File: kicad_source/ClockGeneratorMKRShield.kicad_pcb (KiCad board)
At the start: 2 copper layers, 60 x 23 mm, 3 parts, among them CN1 ARDUINO_MKR

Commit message: generated layout
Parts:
- added C1: 6.8 pF, capacitors:C_0603, F.Cu at (120.0, 167.5)
- added C10: C_0603, capacitors:C_0603, F.Cu at (89.0, 164.5)
- added C11: C_0603, capacitors:C_0603, F.Cu at (94.0, 155.0)
- added C13: C_0603, capacitors:C_0603, F.Cu at (81.0, 167.5)
- added C14: C_0603, capacitors:C_0603, F.Cu at (86.0, 158.5)
- added C16: C_0603, capacitors:C_0603, F.Cu at (72.0, 165.0)
- added C17: C_0603, capacitors:C_0603, F.Cu at (75.3, 155.4)
- added C2: 6.8 pF, capacitors:C_0603, F.Cu at (120.0, 161.5)
- added C3: 100 nF, capacitors:C_0603, F.Cu at (112.0, 161.0)
- added C4: C_0603, capacitors:C_0603, F.Cu at (100.5, 167.5)
- added C5: C_0603, capacitors:C_0603, F.Cu at (105.5, 158.5)
- added C6: C_0603, capacitors:C_0603, F.Cu at (109.4, 158.1)
- added C7: C_0603, capacitors:C_0603, F.Cu at (98.0, 166.5)
- added C8: C_0603, capacitors:C_0603, F.Cu at (103.0, 157.0)
- added CN2: 60312202114509, CON_wuerth:WR-SMA-PCB, F.Cu at (64.0, 162.5)
- added CN3: 60312202114509, CON_wuerth:WR-SMA-PCB, F.Cu at (75.5, 147.5)
- added L10: INDUCTOR_SMALL, L_filter:WE-CAIR_4248, F.Cu at (81.5, 157.5)
- added L3: INDUCTOR_SMALL, L_filter:WE-CAIR_4248, F.Cu at (93.5, 165.5)
- added L4: INDUCTOR_SMALL, L_filter:WE-CAIR_4248, F.Cu at (98.5, 156.0)
- added L6: INDUCTOR_SMALL, L_filter:WE-CAIR_4248, F.Cu at (85.0, 166.0)
- added L7: INDUCTOR_SMALL, L_filter:WE-CAIR_4248, F.Cu at (90.0, 157.0)
- added L9: INDUCTOR_SMALL, L_filter:WE-CAIR_4248, F.Cu at (76.5, 166.5)
- added R1: 10k, resistors:R_0603, F.Cu at (113.0, 158.0)
- added R2: 10k, resistors:R_0603, F.Cu at (113.0, 156.0)
- added U1: SI5351A, SSOP:MSOP-10_3x3mm_Pitch0.5mm, F.Cu at (113.0, 164.0)
- added W1: TEST_1P, wire_pads:SolderWirePad_single_0-8mmDrill, F.Cu at (108.4, 154.6)
- added Y1: Crystal_SMD_4Pad, crystals:Crystal_SMD_3.2x2.5mm_4Pad, F.Cu at (120.0, 164.5)
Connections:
- CN1 pad 20: (no net) -> I2C_SDA
- CN1 pad 21: (no net) -> I2C_SCL
- CN1 pad 25: (no net) -> GND
- CN1 pad 26: (no net) -> +3V3
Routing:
- net GND: track 0.00 -> 63.1 mm, vias 0 -> 17
- net +3V3: track 0.00 -> 37.1 mm
- net I2C_SCL: track 0.00 -> 21.0 mm
- net I2C_SDA: track 0.00 -> 18.4 mm
- net /CLK0: track 0.00 -> 10.6 mm
- net Net-(C17-Pad2): track 0.00 -> 9.49 mm
- net /CLK1: track 0.00 -> 9.26 mm
- net Net-(C16-Pad2): track 0.00 -> 9.15 mm
- net /XA: track 0.00 -> 8.09 mm
- net Net-(C11-Pad2): track 0.00 -> 6.14 mm
- net /XB: track 0.00 -> 6.08 mm
- net Net-(C10-Pad2): track 0.00 -> 5.93 mm
- net Net-(C14-Pad2): track 0.00 -> 5.59 mm
- net Net-(C13-Pad2): track 0.00 -> 5.59 mm
- net /CLK2: track 0.00 -> 5.26 mm
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- added copper zone on B.Cu, net GND
- added copper zone on F.Cu, net GND

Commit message: added connector for gps module
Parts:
- added CN4: SM04B-SRSS-TB, Connector_JST:JST_SH_SM04B-SRSS-TB_1x04-1MP_P1.00mm_Horizontal, F.Cu at (122.5, 155.0)
- added W2: TEST_1P, wire_pads:SolderWirePad_single_0-8mmDrill, F.Cu at (124.0, 166.0)
- C10, C13: value C_0603 -> 47 pF
- C11, C14: value C_0603 -> 130 pF
- C16, C7: value C_0603 -> 30 pF
- C17, C8: value C_0603 -> 91 pF
- C4, C5, C6: value C_0603 -> 10 nF
- L10, L4, L7: value INDUCTOR_SMALL -> 744912212
- L3, L6, L9: value INDUCTOR_SMALL -> 744912156
- Y1: value Crystal_SMD_4Pad -> RH100-25.000-6-F-1010-TR
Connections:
- CN1 pad 13: (no net) -> /PPS_INT
- CN1 pad 22: (no net) -> /SERIAL_RX
- CN1 pad 23: (no net) -> /SERIAL_TX
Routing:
- net /SERIAL_TX: track 0.00 -> 23.2 mm, vias 0 -> 1
- net /SERIAL_RX: track 0.00 -> 20.3 mm, vias 0 -> 1
- net +3V3: track 37.1 -> 47.8 mm, vias 0 -> 2
- net /PPS_INT: track 0.00 -> 9.46 mm
- net GND: track 63.1 -> 68.2 mm, vias 17 -> 16
- net (no net): vias 0 -> 1

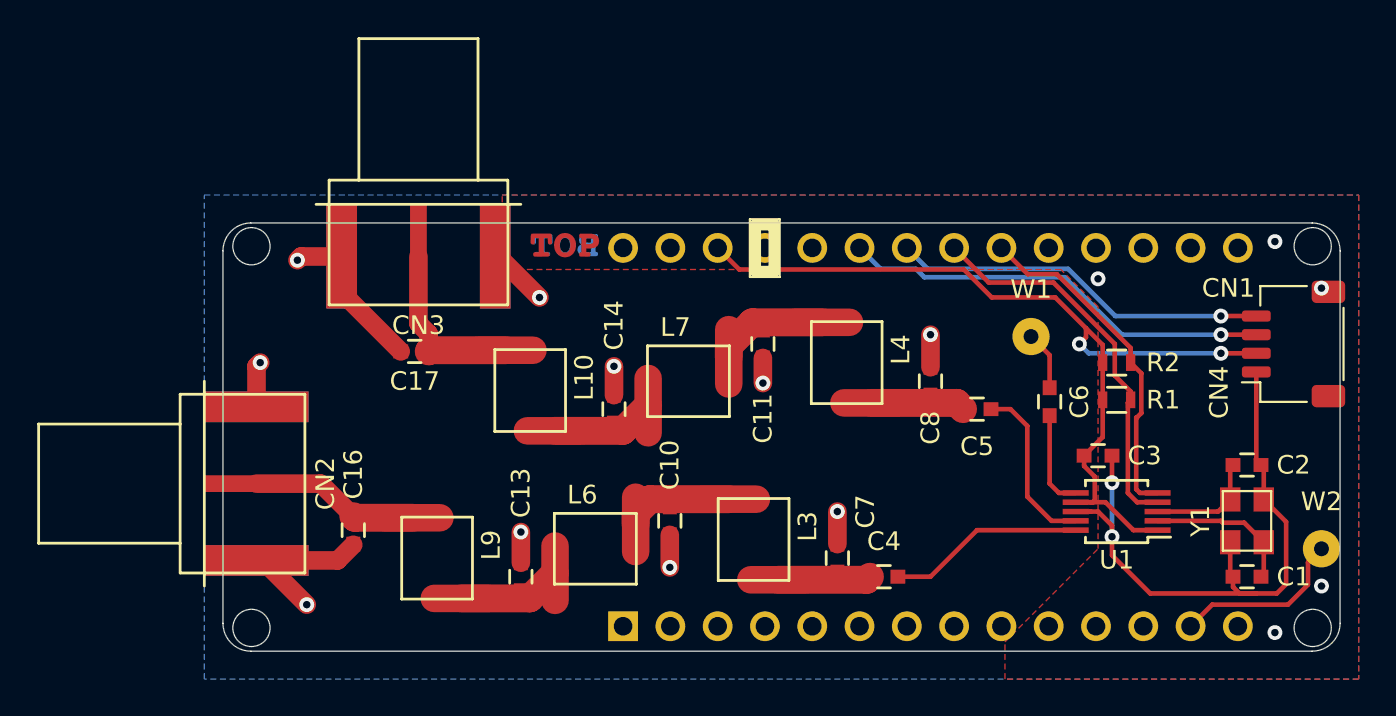
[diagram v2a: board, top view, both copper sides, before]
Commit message: switched to clock generator in QFN package, updated layout
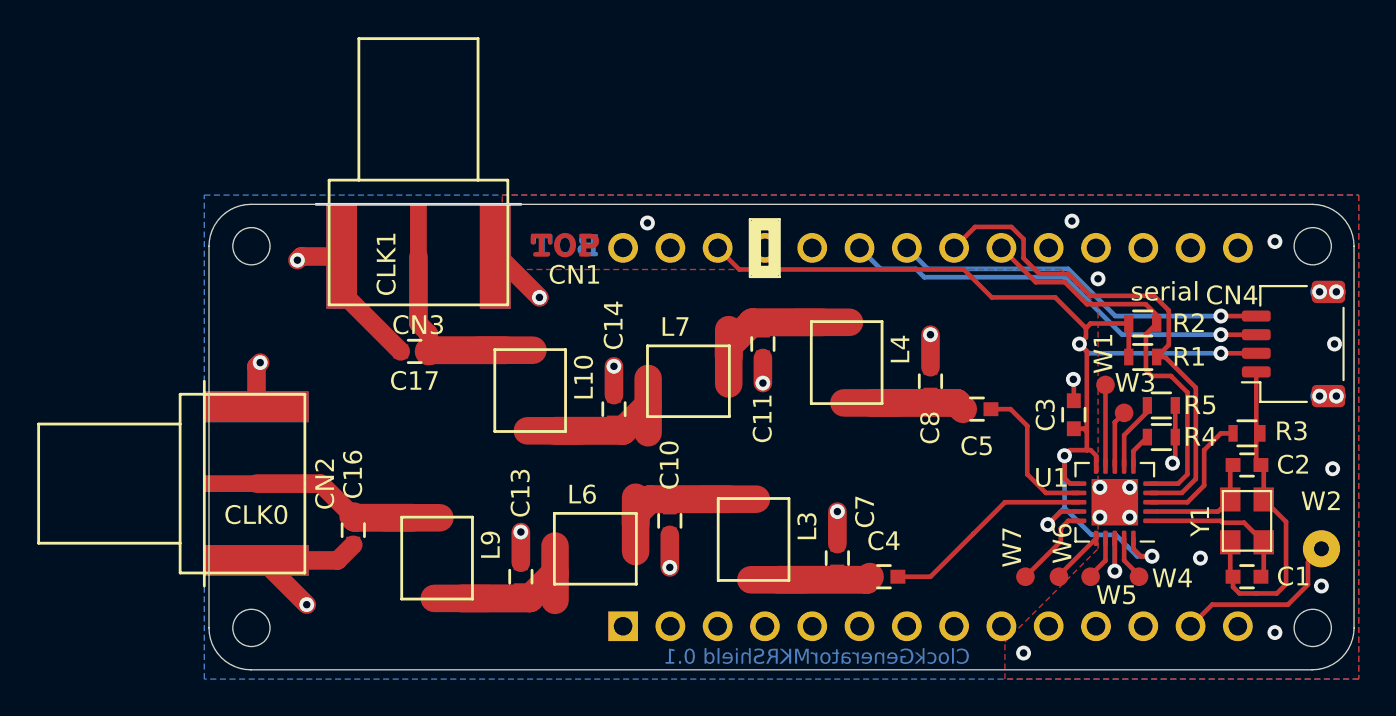
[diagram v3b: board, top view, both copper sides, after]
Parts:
- removed C6: 10 nF, capacitors:C_0603
- added L5: Label, labels:generationmake_small_solder, B.Cu at (124.4, 158.2)
- added L8: Label, labels:generationmake_logo, B.Cu at (96.3, 165.8)
- added R3: 0R, resistors:R_0603, F.Cu at (120.0, 159.8)
- added R4: 0R, resistors:R_0603, F.Cu at (115.4, 160.0)
- added R5: 0R, resistors:R_0603, F.Cu at (115.4, 158.3)
- added W3: TEST_1P, wire_pads:SolderWirePad_single_1mmSMD, F.Cu at (113.4, 158.7)
- added W4: TEST_1P, wire_pads:SolderWirePad_single_1mmSMD, F.Cu at (114.2, 167.5)
- added W5: TEST_1P, wire_pads:SolderWirePad_single_1mmSMD, F.Cu at (111.6, 167.5)
- added W6: TEST_1P, wire_pads:SolderWirePad_single_1mmSMD, F.Cu at (109.9, 167.5)
- added W7: TEST_1P, wire_pads:SolderWirePad_single_1mmSMD, F.Cu at (108.1, 167.5)
- C1, C2: value 6.8 pF -> DNI
- CN2, CN3: value 60312202114509 -> CON-SMA-EDGE-S-ND
- L3, L6, L9: value 744912156 -> 744912212
- U1: value SI5351A -> SI5351A_B_GM; footprint SSOP:MSOP-10_3x3mm_Pitch0.5mm -> QFN:QFN-20-1EP_4x4mm_P0.5mm_EP2.5x2.5mm
- W1: footprint wire_pads:SolderWirePad_single_0-8mmDrill -> wire_pads:SolderWirePad_single_1mmSMD
- moved W1 4.77 mm to (112.4, 157.2)
- moved R1 2.69 mm to (114.4, 155.7)
- moved C3 2.56 mm to (110.7, 158.8), turned to 90 degrees
- moved R2 2.52 mm to (114.4, 153.9)
- moved U1 0.51 mm to (112.9, 163.5)
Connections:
- U1 pad 1: +3V3 -> /XA
- U1 pad 10: /CLK0 -> +3V3
- U1 pad 2: /XA -> /XB
- U1 pad 3: /XB -> /A0
- U1 pad 6: /CLK2 -> /SSEN
- U1 pad 7: +3V3 -> /OEB
- U1 pad 8: GND -> Net-(U1-Pad8)
- U1 pad 9: /CLK1 -> Net-(U1-Pad9)
- W1 pad 1: Net-(C6-Pad1) -> Net-(U1-Pad9)
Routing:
- net +3V3: track 47.8 -> 65.0 mm, vias 2 -> 6
- net GND: track 68.2 -> 60.2 mm, vias 16 -> 26
- net /A0: track 0.00 -> 7.06 mm
- net I2C_SCL: track 21.0 -> 27.6 mm
- net /CLK2: track 5.26 -> 0.00 mm
- net Net-(U1-Pad15): track 0.00 -> 4.52 mm
- net Net-(U1-Pad9): track 0.00 -> 4.36 mm
- net I2C_SDA: track 18.4 -> 22.3 mm
- net /OEB: track 0.00 -> 3.78 mm
- net Net-(C6-Pad1): track 3.16 -> 0.00 mm
- net Net-(U1-Pad8): track 0.00 -> 3.07 mm
- net Net-(U1-Pad16): track 0.00 -> 2.89 mm
- net Net-(U1-Pad17): track 0.00 -> 2.39 mm
- net Net-(U1-Pad19): track 0.00 -> 2.39 mm
- net /SSEN: track 0.00 -> 1.87 mm
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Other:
- board size 60 x 23 mm -> 61.5 x 25 mm
- board text added: "CLK0"
- board text added: "CLK1"
- board text added: "ClockGeneratorMKRShield 0.1"
- board text added: "serial"
